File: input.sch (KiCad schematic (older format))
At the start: 6 parts

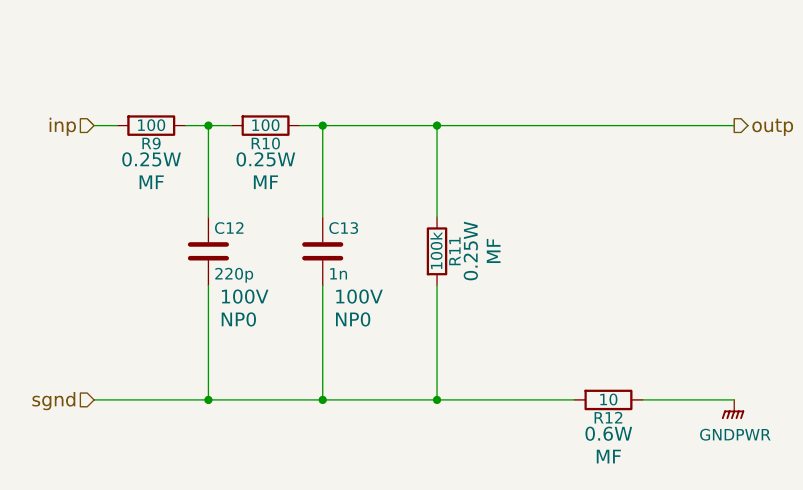
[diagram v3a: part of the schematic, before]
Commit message: Releasing version with distant psu caps.
Signed-off-by: Nenad Radulovic <nenad.b.radulovic@gmail.com>
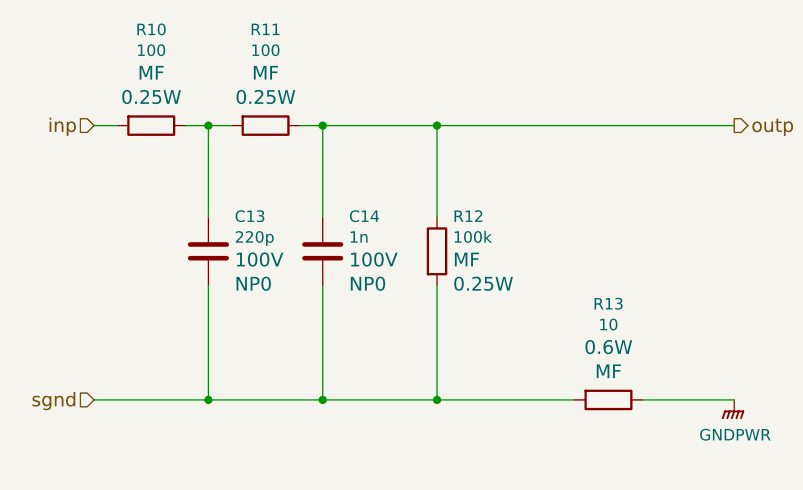
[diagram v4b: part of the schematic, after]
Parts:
- renumbered C12 to C13, C13 to C14, R9 to R10, R10 to R11, R11 to R12, R12 to R13
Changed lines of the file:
@@
 $EndDescr
 $Comp
-L Device:C C13
+L Device:C C14
 U 1 1 5ABB3781
 P 2100 2550
-F 0 "C13" H 2125 2650 50  0000 L CNN
-F 1 "1n" H 2125 2450 50  0000 L CNN
+F 0 "C14" H 2215 2702 50  0000 L CNN
+F 1 "1n" H 2215 2611 50  0000 L CNN
 F 2 "Capacitor_THT:C_Disc_D4.3mm_W1.9mm_P5.00mm" H 2138 2400 50  0001 C CNN
 F 3 "http://www.farnell.com/datasheets/2095938.pdf" H 2100 2550 50  0001 C CNN
-F 4 "100V" H 2150 2350 60  0000 L CNN "Voltage"
-F 5 "NP0" H 2150 2250 60  0000 L CNN "Type"
+F 4 "100V" H 2215 2512 60  0000 L CNN "Voltage"
+F 5 "NP0" H 2215 2406 60  0000 L CNN "Type"
 F 6 "Farnell:1100513" H 2100 2550 60  0001 C CNN "Vendor"
 F 7 "AVX:SR211A102KAR" H 2100 2550 60  0001 C CNN "Manufacturer"
@@
 $EndComp
 $Comp
-L Device:C C12
+L Device:C C13
 U 1 1 5ABB3BB0
 P 1600 2550
-F 0 "C12" H 1625 2650 50  0000 L CNN
-F 1 "220p" H 1625 2450 50  0000 L CNN
+F 0 "C13" H 1715 2702 50  0000 L CNN
+F 1 "220p" H 1715 2611 50  0000 L CNN
 F 2 "Capacitor_THT:C_Disc_D4.3mm_W1.9mm_P5.00mm" H 1638 2400 50  0001 C CNN
 F 3 "http://www.farnell.com/datasheets/2095938.pdf" H 1600 2550 50  0001 C CNN
-F 4 "100V" H 1650 2350 60  0000 L CNN "Voltage"
-F 5 "NP0" H 1650 2250 60  0000 L CNN "Type"
+F 4 "100V" H 1715 2512 60  0000 L CNN "Voltage"
+F 5 "NP0" H 1715 2406 60  0000 L CNN "Type"
 F 6 "Farnell:1100508" H 1600 2550 60  0001 C CNN "Vendor"
 F 7 "AVX:SR211A221JAR" H 1600 2550 60  0001 C CNN "Manufacturer"
@@
 outp
 $Comp
-L Device:R R9
+L Device:R R10
 U 1 1 5AD6B4EC
 P 1350 2000
-F 0 "R9" V 1430 2000 50  0000 C CNN
-F 1 "100" V 1350 2000 50  0000 C CNN
+F 0 "R10" V 931 2000 50  0000 C CNN
+F 1 "100" V 1022 2000 50  0000 C CNN
 F 2 "Resistor_THT:R_Axial_DIN0207_L6.3mm_D2.5mm_P10.16mm_Horizontal" V 1280 2000 50  0001 C CNN
 F 3 "http://www.farnell.com/datasheets/1723855.pdf" H 1350 2000 50  0001 C CNN
 F 4 "Farnell:2329854" V 1350 2000 60  0001 C CNN "Vendor"
 F 5 "TE Connectivity:LR0204F100R" V 1350 2000 60  0001 C CNN "Manufacturer"
-F 6 "MF" V 1600 2000 60  0000 C CNN "Type"
-F 7 "0.25W" V 1500 2000 60  0000 C CNN "Power"
+F 6 "MF" V 1121 2000 60  0000 C CNN "Type"
+F 7 "0.25W" V 1227 2000 60  0000 C CNN "Power"
 	1    1350 2000
 	0    1    1    0
 $EndComp
 $Comp
-L Device:R R10
+L Device:R R11
 U 1 1 5AD70334
 P 1850 2000
-F 0 "R10" V 1930 2000 50  0000 C CNN
-F 1 "100" V 1850 2000 50  0000 C CNN
+F 0 "R11" V 1431 2000 50  0000 C CNN
+F 1 "100" V 1522 2000 50  0000 C CNN
 F 2 "Resistor_THT:R_Axial_DIN0207_L6.3mm_D2.5mm_P10.16mm_Horizontal" V 1780 2000 50  0001 C CNN
 F 3 "http://www.farnell.com/datasheets/1723855.pdf" H 1850 2000 50  0001 C CNN
 F 4 "Farnell:2329854" V 1850 2000 60  0001 C CNN "Vendor"
 F 5 "TE Connectivity:LR0204F100R" V 1850 2000 60  0001 C CNN "Manufacturer"
-F 6 "MF" V 2100 2000 60  0000 C CNN "Type"
-F 7 "0.25W" V 2000 2000 60  0000 C CNN "Power"
+F 6 "MF" V 1621 2000 60  0000 C CNN "Type"
+F 7 "0.25W" V 1727 2000 60  0000 C CNN "Power"
 	1    1850 2000
 	0    1    1    0
 $EndComp
 $Comp
-L Device:R R12
+L Device:R R13
 U 1 1 5B193CC4
 P 3350 3200
-F 0 "R12" V 3430 3200 50  0000 C CNN
-F 1 "10" V 3350 3200 50  0000 C CNN
+F 0 "R13" V 2931 3200 50  0000 C CNN
+F 1 "10" V 3022 3200 50  0000 C CNN
 F 2 "Resistor_THT:R_Axial_DIN0207_L6.3mm_D2.5mm_P10.16mm_Horizontal" V 3280 3200 50  0001 C CNN
 F 3 "http://www.farnell.com/datasheets/1723855.pdf" H 3350 3200 50  0001 C CNN
 F 4 "Farnell:2329993" V 3350 3200 60  0001 C CNN "Vendor"
 F 5 "TE Connectivity:LR1F10R" V 3350 3200 60  0001 C CNN "Manufacturer"
-F 6 "0.6W" V 3500 3200 60  0000 C CNN "Power"
-F 7 "MF" V 3600 3200 60  0000 C CNN "Type"
+F 6 "0.6W" V 3121 3200 60  0000 C CNN "Power"
+F 7 "MF" V 3227 3200 60  0000 C CNN "Type"
 	1    3350 3200
 	0    1    1    0
@@
 	2600 2700 2600 3200
 $Comp
-L Device:R R11
+L Device:R R12
 U 1 1 5AD713B4
 P 2600 2550
-F 0 "R11" V 2680 2550 50  0000 C CNN
-F 1 "100k" V 2600 2550 50  0000 C CNN
+F 0 "R12" H 2670 2702 50  0000 L CNN
+F 1 "100k" H 2670 2611 50  0000 L CNN
 F 2 "Resistor_THT:R_Axial_DIN0207_L6.3mm_D2.5mm_P10.16mm_Horizontal" V 2530 2550 50  0001 C CNN
 F 3 "http://www.farnell.com/datasheets/1723855.pdf" H 2600 2550 50  0001 C CNN
 F 4 "Farnell:2329853" V 2600 2550 60  0001 C CNN "Vendor"
 F 5 "TE Connectivity:LR0204F100K" V 2600 2550 60  0001 C CNN "Manufacturer"
-F 6 "MF" V 2850 2550 60  0000 C CNN "Type"
-F 7 "0.25W" V 2750 2550 60  0000 C CNN "Power"
+F 6 "MF" H 2670 2512 60  0000 L CNN "Type"
+F 7 "0.25W" H 2670 2406 60  0000 L CNN "Power"
 	1    2600 2550
 	1    0    0    -1
@@
 sgnd
 $Comp
-L power:GNDPWR #PWR015
+L power:GNDPWR #PWR016
 U 1 1 5B618F0C
 P 3900 3200
-F 0 "#PWR015" H 3900 3000 50  0001 C CNN
+F 0 "#PWR016" H 3900 3000 50  0001 C CNN
 F 1 "GNDPWR" H 3904 3046 50  0000 C CNN
 F 2 "" H 3900 3150 50  0001 C CNN

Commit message: Relase v1.0
Corrected a few things on the PCB.
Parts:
- C14: value 1n -> 2n2; Manufacturer AVX:SR211A102KAR -> SR211A222JAR; Vendor Farnell:1100513 -> Farnell:1100515
- R10, R11, R12: footprint Resistor_THT:R_Axial_DIN0207_L6.3mm_D2.5mm_P10.16mm_Horizontal -> Resistor_THT:R_Axial_DIN0207_L6.3mm_D2.5mm_P7.62mm_Horizontal
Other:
- note added: "Put R10 and C13 right next to\ninput connector. The return\nground should be at the connector\nside."
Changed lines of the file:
@@
 P 2100 2550
 F 0 "C14" H 2215 2702 50  0000 L CNN
-F 1 "1n" H 2215 2611 50  0000 L CNN
+F 1 "2n2" H 2215 2611 50  0000 L CNN
 F 2 "Capacitor_THT:C_Disc_D4.3mm_W1.9mm_P5.00mm" H 2138 2400 50  0001 C CNN
 F 3 "http://www.farnell.com/datasheets/2095938.pdf" H 2100 2550 50  0001 C CNN
 F 4 "100V" H 2215 2512 60  0000 L CNN "Voltage"
 F 5 "NP0" H 2215 2406 60  0000 L CNN "Type"
-F 6 "Farnell:1100513" H 2100 2550 60  0001 C CNN "Vendor"
-F 7 "AVX:SR211A102KAR" H 2100 2550 60  0001 C CNN "Manufacturer"
+F 6 "Farnell:1100515" H 2100 2550 60  0001 C CNN "Vendor"
+F 7 "SR211A222JAR" H 2100 2550 60  0001 C CNN "Manufacturer"
 	1    2100 2550
 	1    0    0    -1
@@
 F 0 "R10" V 931 2000 50  0000 C CNN
 F 1 "100" V 1022 2000 50  0000 C CNN
-F 2 "Resistor_THT:R_Axial_DIN0207_L6.3mm_D2.5mm_P10.16mm_Horizontal" V 1280 2000 50  0001 C CNN
+F 2 "Resistor_THT:R_Axial_DIN0207_L6.3mm_D2.5mm_P7.62mm_Horizontal" V 1280 2000 50  0001 C CNN
 F 3 "http://www.farnell.com/datasheets/1723855.pdf" H 1350 2000 50  0001 C CNN
 F 4 "Farnell:2329854" V 1350 2000 60  0001 C CNN "Vendor"
@@
 F 0 "R11" V 1431 2000 50  0000 C CNN
 F 1 "100" V 1522 2000 50  0000 C CNN
-F 2 "Resistor_THT:R_Axial_DIN0207_L6.3mm_D2.5mm_P10.16mm_Horizontal" V 1780 2000 50  0001 C CNN
+F 2 "Resistor_THT:R_Axial_DIN0207_L6.3mm_D2.5mm_P7.62mm_Horizontal" V 1780 2000 50  0001 C CNN
 F 3 "http://www.farnell.com/datasheets/1723855.pdf" H 1850 2000 50  0001 C CNN
 F 4 "Farnell:2329854" V 1850 2000 60  0001 C CNN "Vendor"
@@
 F 0 "R12" H 2670 2702 50  0000 L CNN
 F 1 "100k" H 2670 2611 50  0000 L CNN
-F 2 "Resistor_THT:R_Axial_DIN0207_L6.3mm_D2.5mm_P10.16mm_Horizontal" V 2530 2550 50  0001 C CNN
+F 2 "Resistor_THT:R_Axial_DIN0207_L6.3mm_D2.5mm_P7.62mm_Horizontal" V 2530 2550 50  0001 C CNN
 F 3 "http://www.farnell.com/datasheets/1723855.pdf" H 2600 2550 50  0001 C CNN
 F 4 "Farnell:2329853" V 2600 2550 60  0001 C CNN "Vendor"
@@
 Wire Wire Line
 	2600 3200 3200 3200
+Text Notes 1050 3650 0    50   ~ 0
+Put R10 and C13 right next to\ninput connector. The return\nground should be at the connector\nside.
 $EndSCHEMATC
